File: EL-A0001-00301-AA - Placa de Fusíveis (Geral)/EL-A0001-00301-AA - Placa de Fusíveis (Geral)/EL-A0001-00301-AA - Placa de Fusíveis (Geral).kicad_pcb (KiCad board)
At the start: 2 copper layers, 30 parts, among them J1 1-776087-1, J10 AUX_POWER, J2 AUX_1, J3 AUX_2, J4 DC_CONVERTER, J5 VBAT, J6 UNFUSED, J7 CS_POWER, J8 ECU_POWER, J9 ISOL_POWER, U1 TJA1050-Module

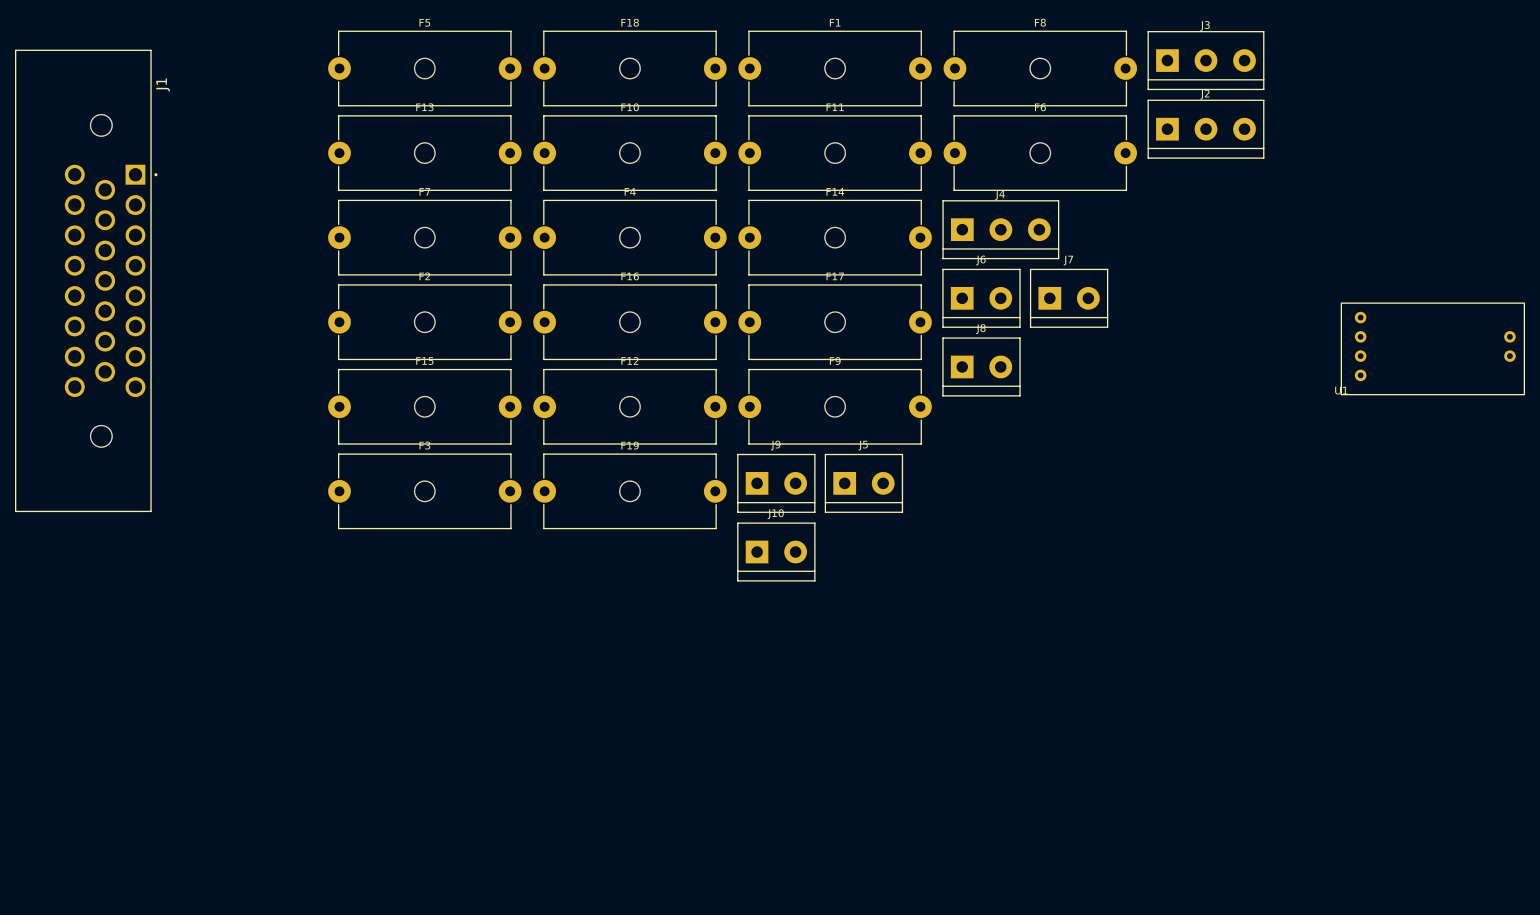
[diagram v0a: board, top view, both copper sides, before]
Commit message: MOD: placa de fusiveis
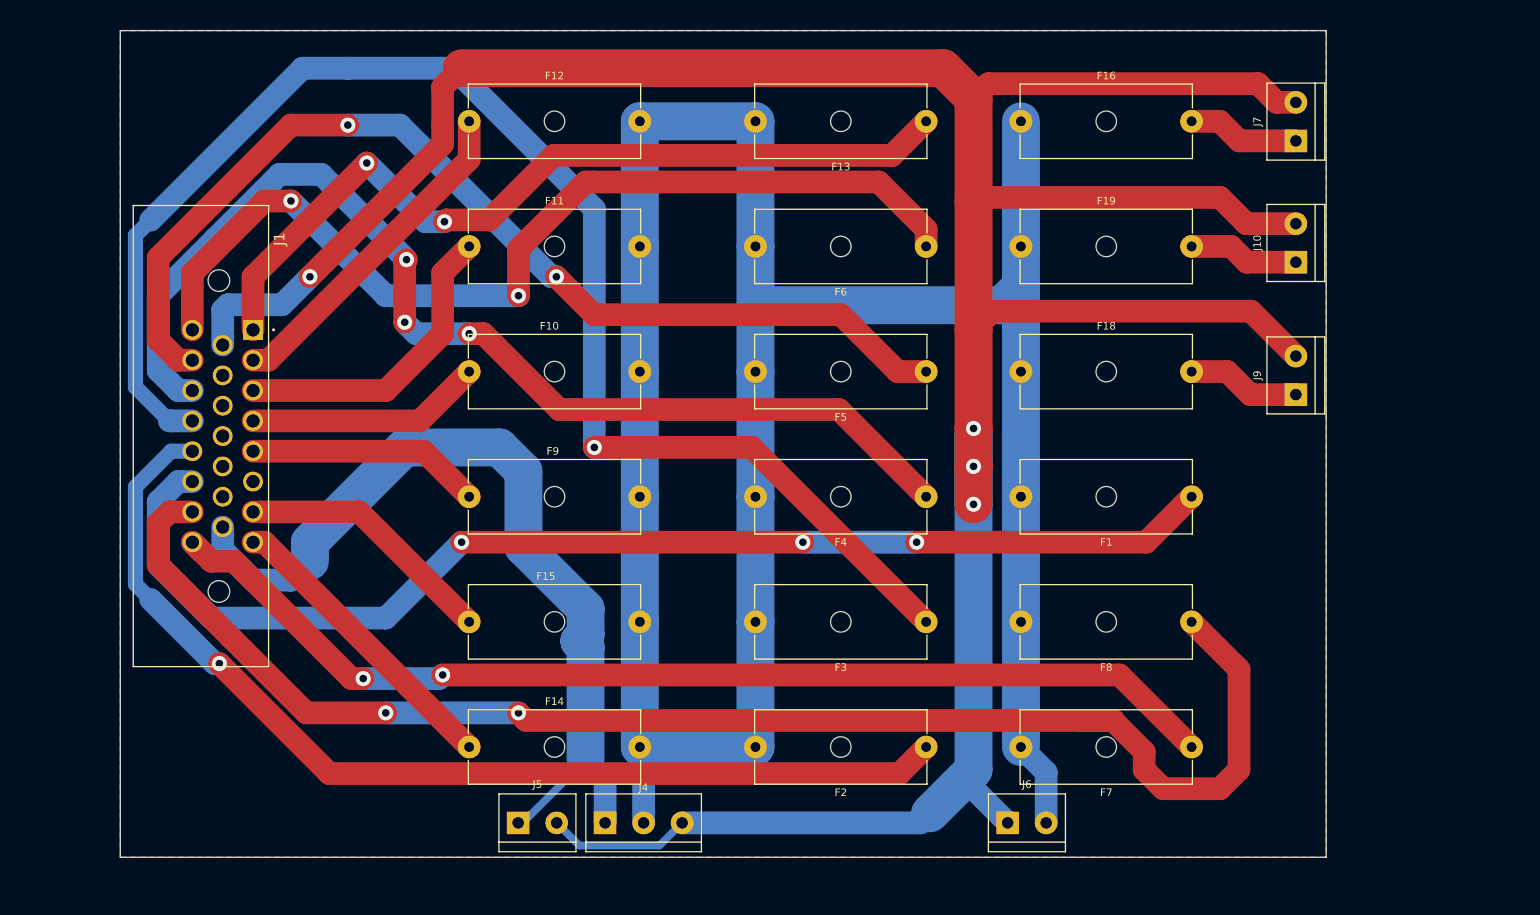
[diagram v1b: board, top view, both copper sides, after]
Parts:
- removed F17: Fuse, Fuse:Fuseholder_Cylinder-5x20mm_Schurter_0031_8201_Horizontal_Open
- removed J2: AUX_1, TerminalBlock:TerminalBlock_bornier-3_P5.08mm
- removed J3: AUX_2, TerminalBlock:TerminalBlock_bornier-3_P5.08mm
- removed J8: ECU_POWER, TerminalBlock:TerminalBlock_bornier-2_P5.08mm
- removed U1: TJA1050-Module, Cheetah:TJA1050-Module
- moved F7 130.9 mm to (170.2, 132.5), turned to 180 degrees
- moved F2 95.5 mm to (135.2, 132.5), turned to 180 degrees
- moved J4 91.3 mm to (92.9, 142.5)
- moved F5 87.1 mm to (135.2, 83.0), turned to 180 degrees
- moved F1 81.1 mm to (170.2, 99.5), turned to 180 degrees
- moved J10 80.7 mm to (184.0, 68.5), turned to 90 degrees
- moved F8 79.4 mm to (170.2, 116.0), turned to 180 degrees
- moved F3 79.2 mm to (135.2, 116.0), turned to 180 degrees
- moved F13 77.5 mm to (135.2, 50.0), turned to 180 degrees
- moved F14 76.7 mm to (75.0, 132.5)
- moved F18 74.4 mm to (147.8, 83.0)
- moved J9 72.0 mm to (184.0, 86.0), turned to 90 degrees
- moved F19 70.6 mm to (147.8, 66.5)
- moved J6 69.4 mm to (146.0, 142.5)
- moved F16 68.2 mm to (147.8, 50.0)
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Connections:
- F11 pad 1: Net-(F11-Pad1) -> Net-(J1-Pad3)
- F12 pad 1: Net-(F12-Pad1) -> Net-(J1-Pad2)
- F13 pad 1: Net-(F13-Pad1) -> Net-(J1-Pad1)
- F7 pad 1: Net-(F7-Pad1) -> Net-(J1-Pad23)
- F8 pad 1: Net-(F8-Pad1) -> Net-(J1-Pad22)
- J1 pad 10: Net-(F12-Pad1) -> unconnected-(J1-Pad10)
- J1 pad 11: Net-(F11-Pad1) -> unconnected-(J1-Pad11)
- J1 pad 12: Net-(F10-Pad1) -> unconnected-(J1-Pad12)
- J1 pad 13: Net-(F9-Pad1) -> unconnected-(J1-Pad13)
- J1 pad 14: Net-(F8-Pad1) -> unconnected-(J1-Pad14)
- J1 pad 15: Net-(F7-Pad1) -> Net-(J1-Pad15)
- J1 pad 22: GNDREF -> Net-(J1-Pad22)
- J1 pad 4: Net-(J1-Pad4) -> Net-(F10-Pad1)
- J1 pad 5: Net-(J1-Pad5) -> Net-(F9-Pad1)
- J1 pad 6: Net-(J1-Pad6) -> unconnected-(J1-Pad6)
- J1 pad 9: Net-(F13-Pad1) -> GNDREF
- J4 pad 1: Net-(J1-Pad23) -> Net-(J1-Pad15)
- J4 pad 2: GNDREF -> 12V
- J4 pad 3: 12V -> GNDREF
- J5 pad 1: Net-(J1-Pad23) -> Net-(J1-Pad15)
- J6 pad 1: 12V -> GNDREF
- J6 pad 2: GNDREF -> 12V
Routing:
- net GNDREF: track 0.00 -> 424.9 mm, vias 0 -> 4
- net 12V: track 0.00 -> 335.6 mm
- net Net-(J1-Pad22): track 0.00 -> 194.4 mm, vias 0 -> 2
- net Net-(F3-Pad1): track 0.00 -> 191.4 mm, vias 0 -> 1
- net Net-(F1-Pad1): track 0.00 -> 159.7 mm, vias 0 -> 3
- net Net-(F4-Pad1): track 0.00 -> 145.8 mm, vias 0 -> 3
- net Net-(J1-Pad23): track 0.00 -> 145.2 mm, vias 0 -> 2
- net Net-(J1-Pad17): track 0.00 -> 138.4 mm, vias 0 -> 2
- net Net-(F2-Pad1): track 0.00 -> 138.3 mm, vias 0 -> 1
- net Net-(F6-Pad1): track 0.00 -> 128.0 mm, vias 0 -> 2
- net Net-(J1-Pad15): track 0.00 -> 118.1 mm
- net Net-(J1-Pad1): track 0.00 -> 110.7 mm, vias 0 -> 2
- net Net-(J1-Pad2): track 0.00 -> 44.5 mm
- net Net-(J1-Pad3): track 0.00 -> 41.1 mm
- net Net-(F14-Pad1): track 0.00 -> 39.7 mm
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- added copper zone on B.Cu, net 12V
- added copper zone on F.Cu, net GNDREF
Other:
- board outline added: 159 x 109 mm
